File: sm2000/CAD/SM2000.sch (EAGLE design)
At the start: 360 parts, among them CN1 HDR100-3, CN10 ST-3509, CN11 HDR100-3, CN2 JS-MU3-002, CN3 DS-0518, CN5 ST-3509, CN8 ST-3509, J1 JMP-2PIN, J2 JMP-2PIN, J3 JMP-2PIN, J4 CONN-BOOM-XH-2A, P10 TPAD50, P11 TPAD50, P12 TPAD50, P13 TPAD50, P14 TPAD50, P16 TPAD50, P18 TPAD50, P19 TPAD50, P20 TPAD50, P21 TPAD50, P3 TPAD50, P4 TPAD50, P5 TPAD50, P6 TPAD50, P7 TPAD50, P8 TPAD50, P9 TPAD50, Q1 MMBT3904, Q12 BRF92, Q13 BFQ19, Q14 RD01MUS2, Q17 MMT2904, Q18 MMT2904, Q2 MMBT3904, Q3 MMBT3904, Q4 MMBT3904, Q5 MMBT3904, Q6 MMBT3904, Q7 BC548, Q8 BC549, SW1 SW-LC2259, SW2 TS-026, SW3 SW-LC2259EENP, SW4 TS-026, SW5 TS-02B, U1 STM32F405VGT6, U10 DNL, U12 PGA-103+, U13 ADE-1, U14 SI570CAC000141DG, U15 SI5351A, U3 STMPS2141, U4 EMIF02-USB03F2, U5 TPS54329E, U6 LD3985M33R, U7 SA612A, U8 LM386M-1, U9 LMV341, X1 BU-SMA-H, X2 BU-SMA-H

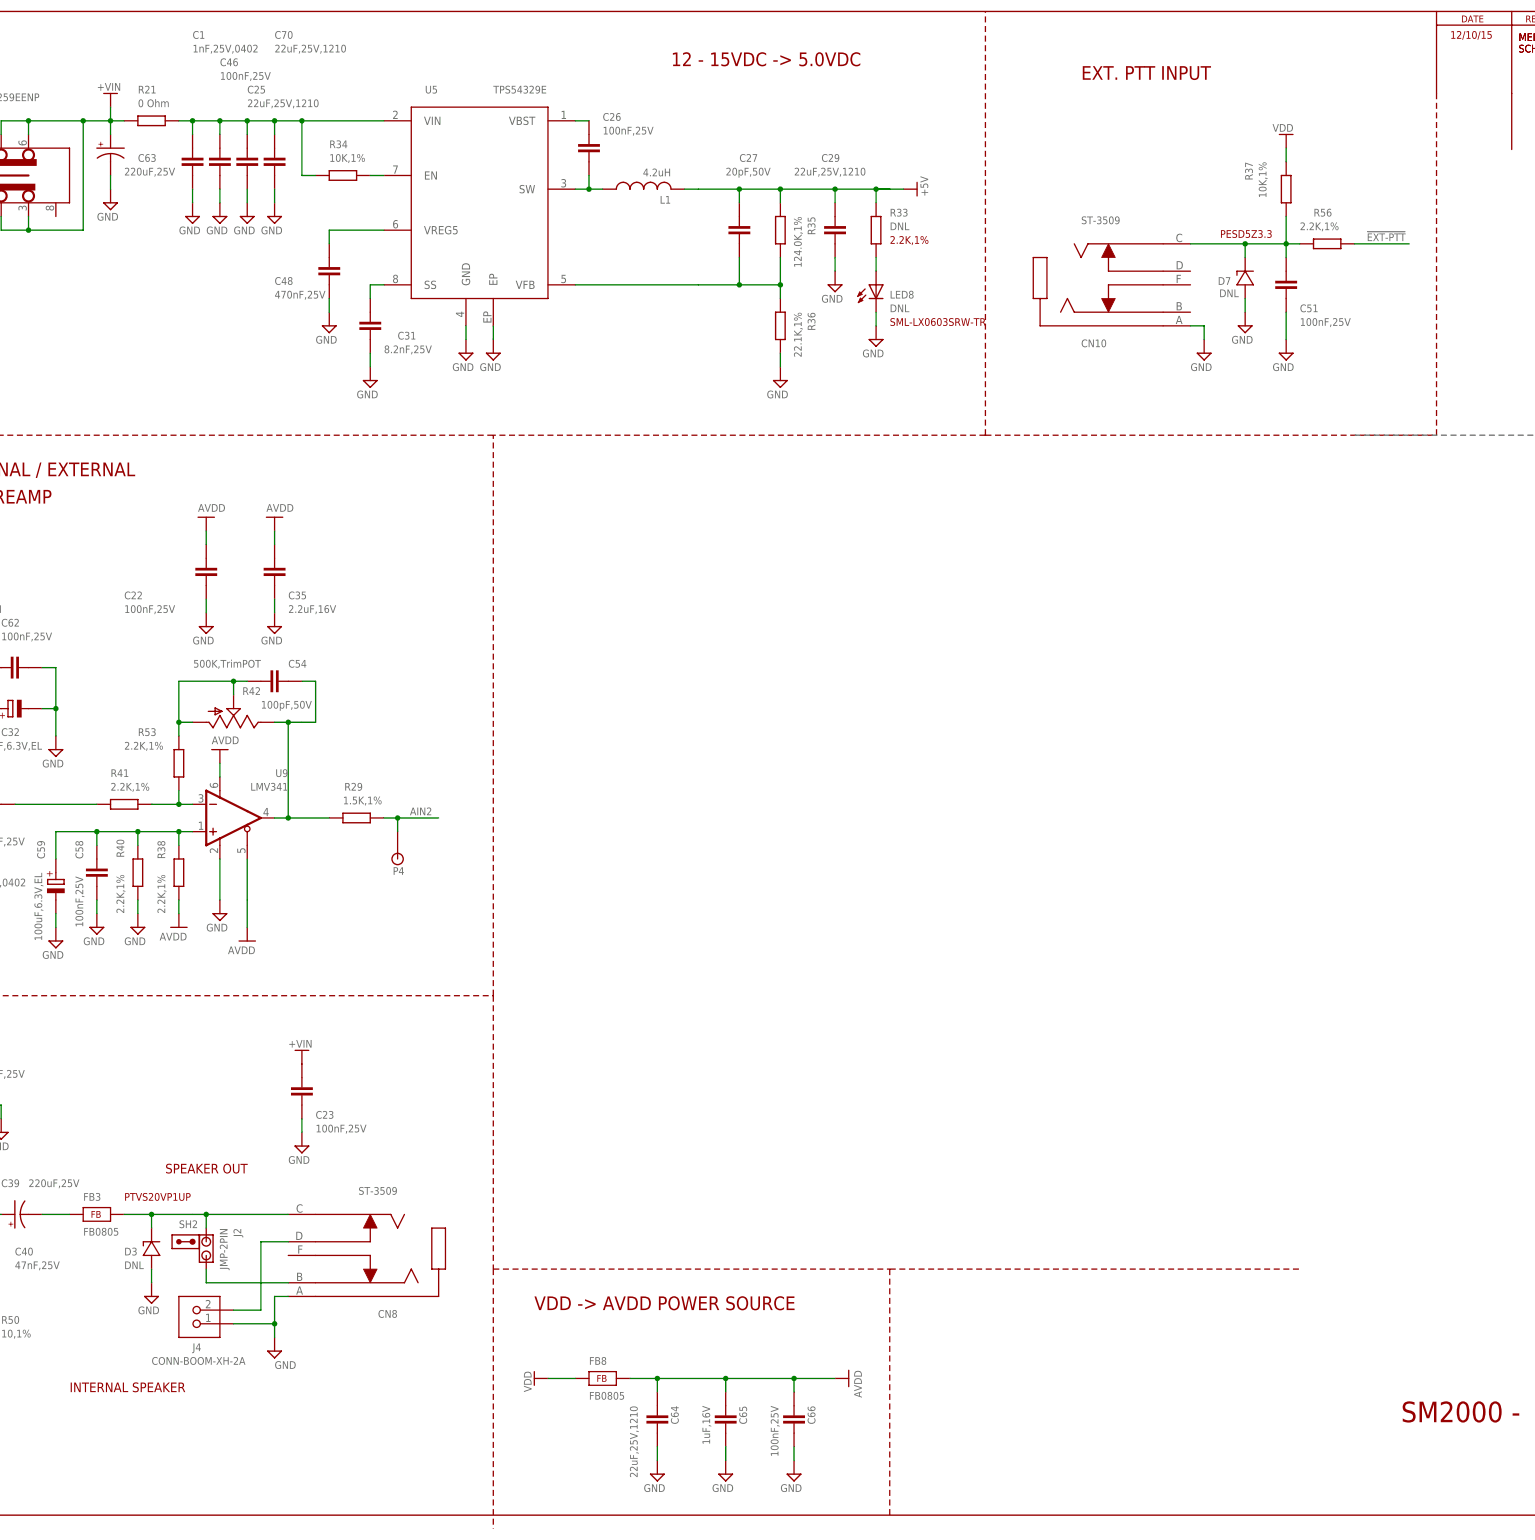
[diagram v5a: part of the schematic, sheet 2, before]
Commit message: Intermediate Schematic Cleanup Added +9, +5 & +3.3V regulators RGB
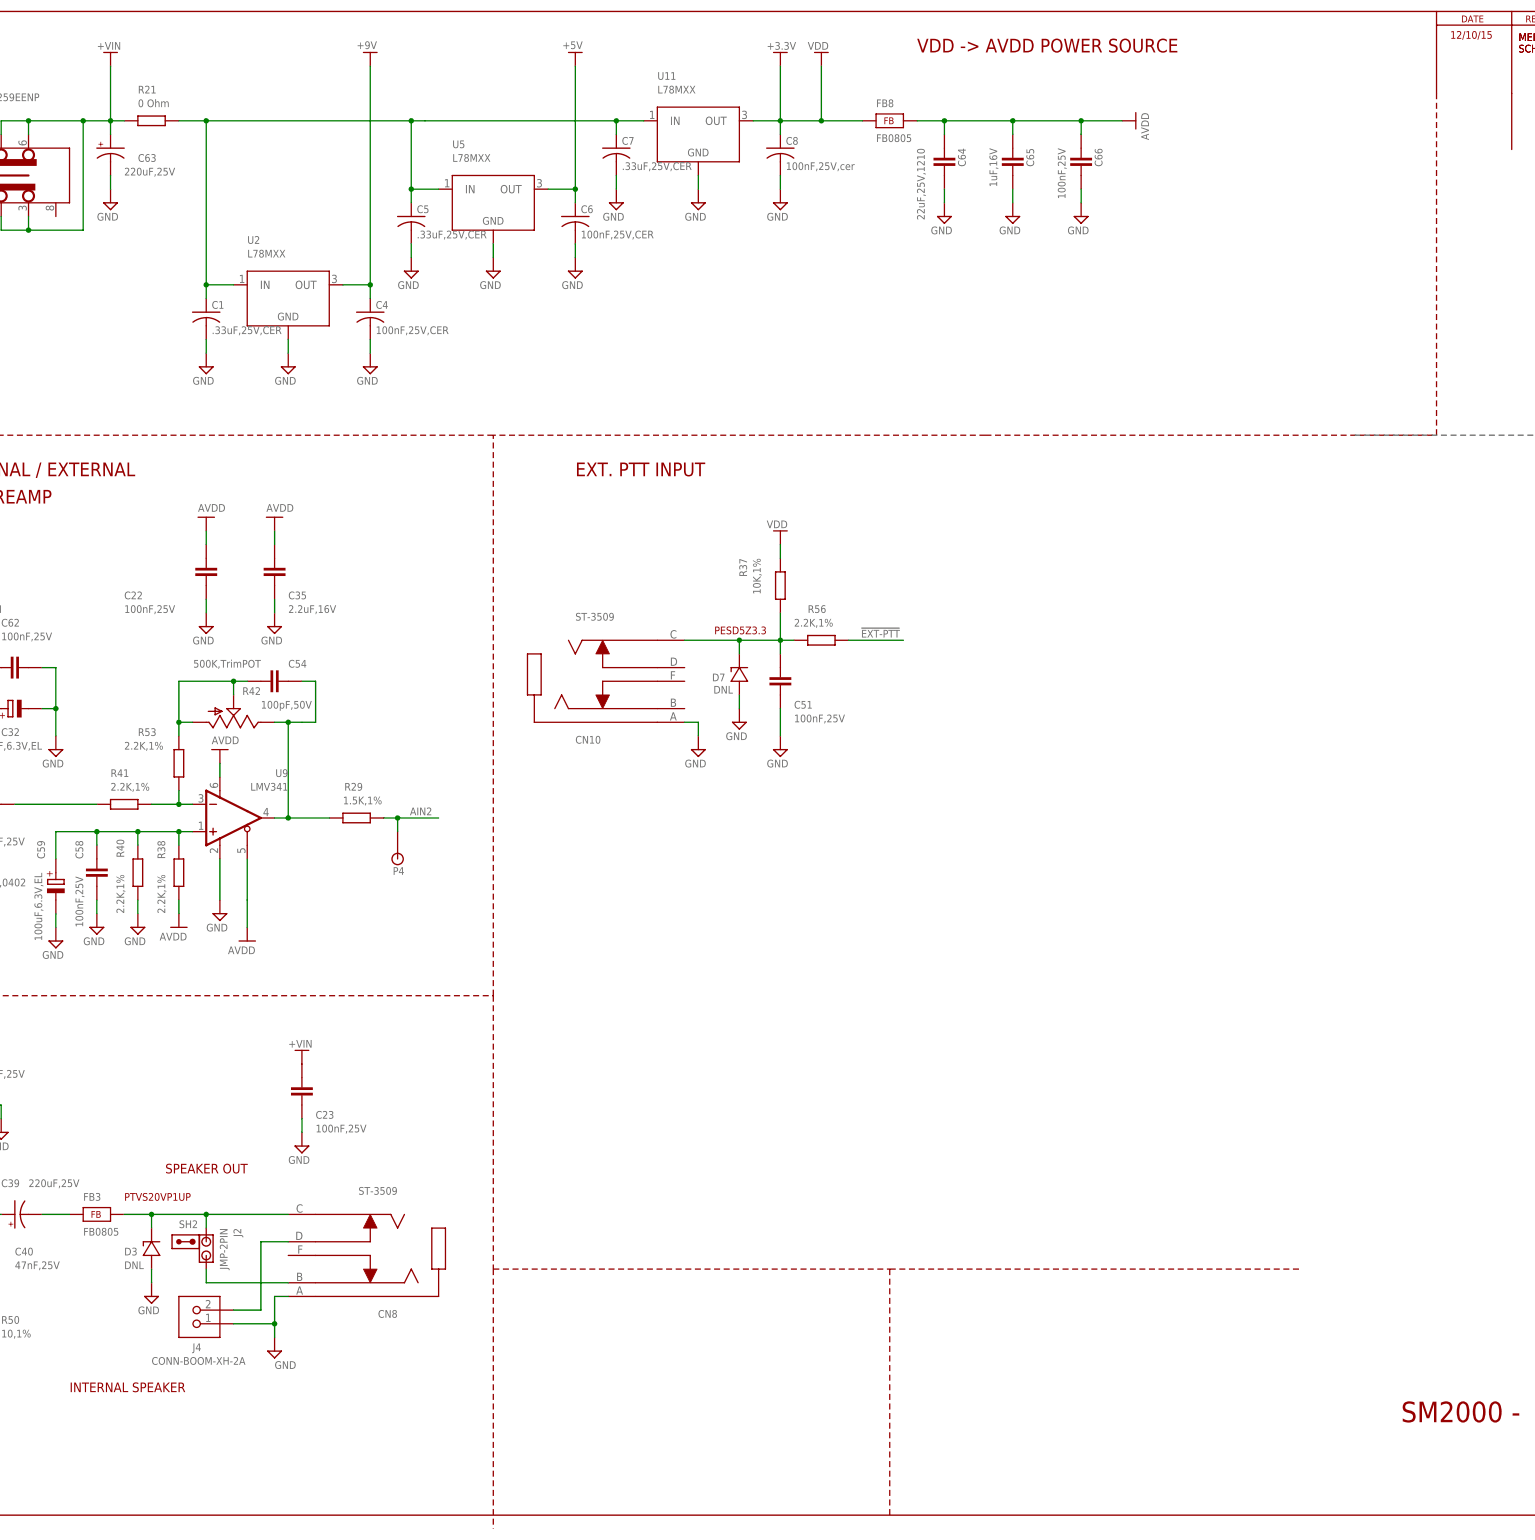
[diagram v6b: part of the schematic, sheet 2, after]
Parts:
- removed C25, C70: 22uF,25V,1210, ipc-7351-capacitor:CAPACITOR_1210
- removed C26, C46: 100nF,25V, AA-ipc-7351-capacitor:CAPACITOR_0402
- removed C27: 20pF,50V, AA-ipc-7351-capacitor:CAPACITOR_0402
- removed C29: 22uF,25V,1210, AA-ipc-7351-capacitor:CAPACITOR_1210
- removed C31: 8.2nF,25V, ipc-7351-capacitor:CAPACITOR_0603
- removed C48: 470nF,25V, ipc-7351-capacitor:CAPACITOR_0603
- removed L1: 4.2uH, _RoweTel:SRR5028
- removed LED8: DNL, _RoweTel:SML-LX0603SRW
- removed R33: DNL, AA-ipc-7351-resistor:RESISTOR_0402
- removed R34: 10K,1%, AA-ipc-7351-resistor:RESISTOR_0402
- removed R35: 124.0K,1%, AA-ipc-7351-resistor:RESISTOR_0402
- removed R36: 22.1K,1%, AA-ipc-7351-resistor:RESISTOR_0402
- added C4, C6: 100nF,25V,CER, _RoweTel:CAP-0805
- added C5, C7: .33uF,25V,CER, _RoweTel:CAP-0805
- added C8: 100nF,25V,cer, _RoweTel:CAP-0805
- added U11, U2: L78MXX, _RoweTel:L78MXX
- C1: value 1nF,25V,0402 -> .33uF,25V,CER; device AA-ipc-7351-capacitor:CAPACITOR_0402 -> _RoweTel:CAP-0805
- U5: value TPS54329E -> L78MXX; device _RoweTel:TPS54329E -> _RoweTel:L78MXX
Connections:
- removed net N$116: L13.1
- removed net N$138: C139.2
- removed net N$155: C147.1, R48.2
- removed net N$21: C26.1, U5.VBST
- removed net N$30: C27.2, R35.2, R36.1, U5.VFB
- removed net N$36: C1.2, C25.1, C46.1, C70.1, R21.2, R34.1, U5.VIN
- removed net N$38: C31.1, U5.SS
- removed net N$40: C48.1, U5.VREG5
- removed net N$42: R34.2, U5.EN
- removed net N$47: LED8.A, R33.2
- removed net N$50: U7.IN_B
- removed net SW: C26.2, L1.1, U5.SW
- new net +9V: C4.1, L13.1, U2.OUT
- new net ANT_SMA: C100.1, C147.1, L14.2, R48.2
- new net N$54: C1.1, C5.1, C7.1, R21.2, U11.IN, U2.IN, U5.IN
- net +5V: now also C6.1, U5.OUT; no longer C27.1, C29.1, L1.2, R33.1, R35.1
- net GND: now also C1.2, C4.2, C5.2, C6.2, C7.2, C8.2, U11.GND, U2.GND; no longer C1.1, C25.2, C29.2, C31.2, C46.2, C48.2, C70.2, LED8.C, R36.2, U5.EP
- net N$11: now also C139.2, U12.1N; no longer C100.1, L14.2
- net N$51: now also U7.IN_B
- net VDD: now also C8.1, U11.OUT
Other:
- note removed: "+9V"
- note removed: "12 - 15VDC -> 5.0VDC"
- note removed: "2.2K,1%"
- note removed: "Antenna SMA"
- moved on the sheet: C1, C135, C136, C51, C64, C65, C66, C97, CN10, D7, FB21, FB6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

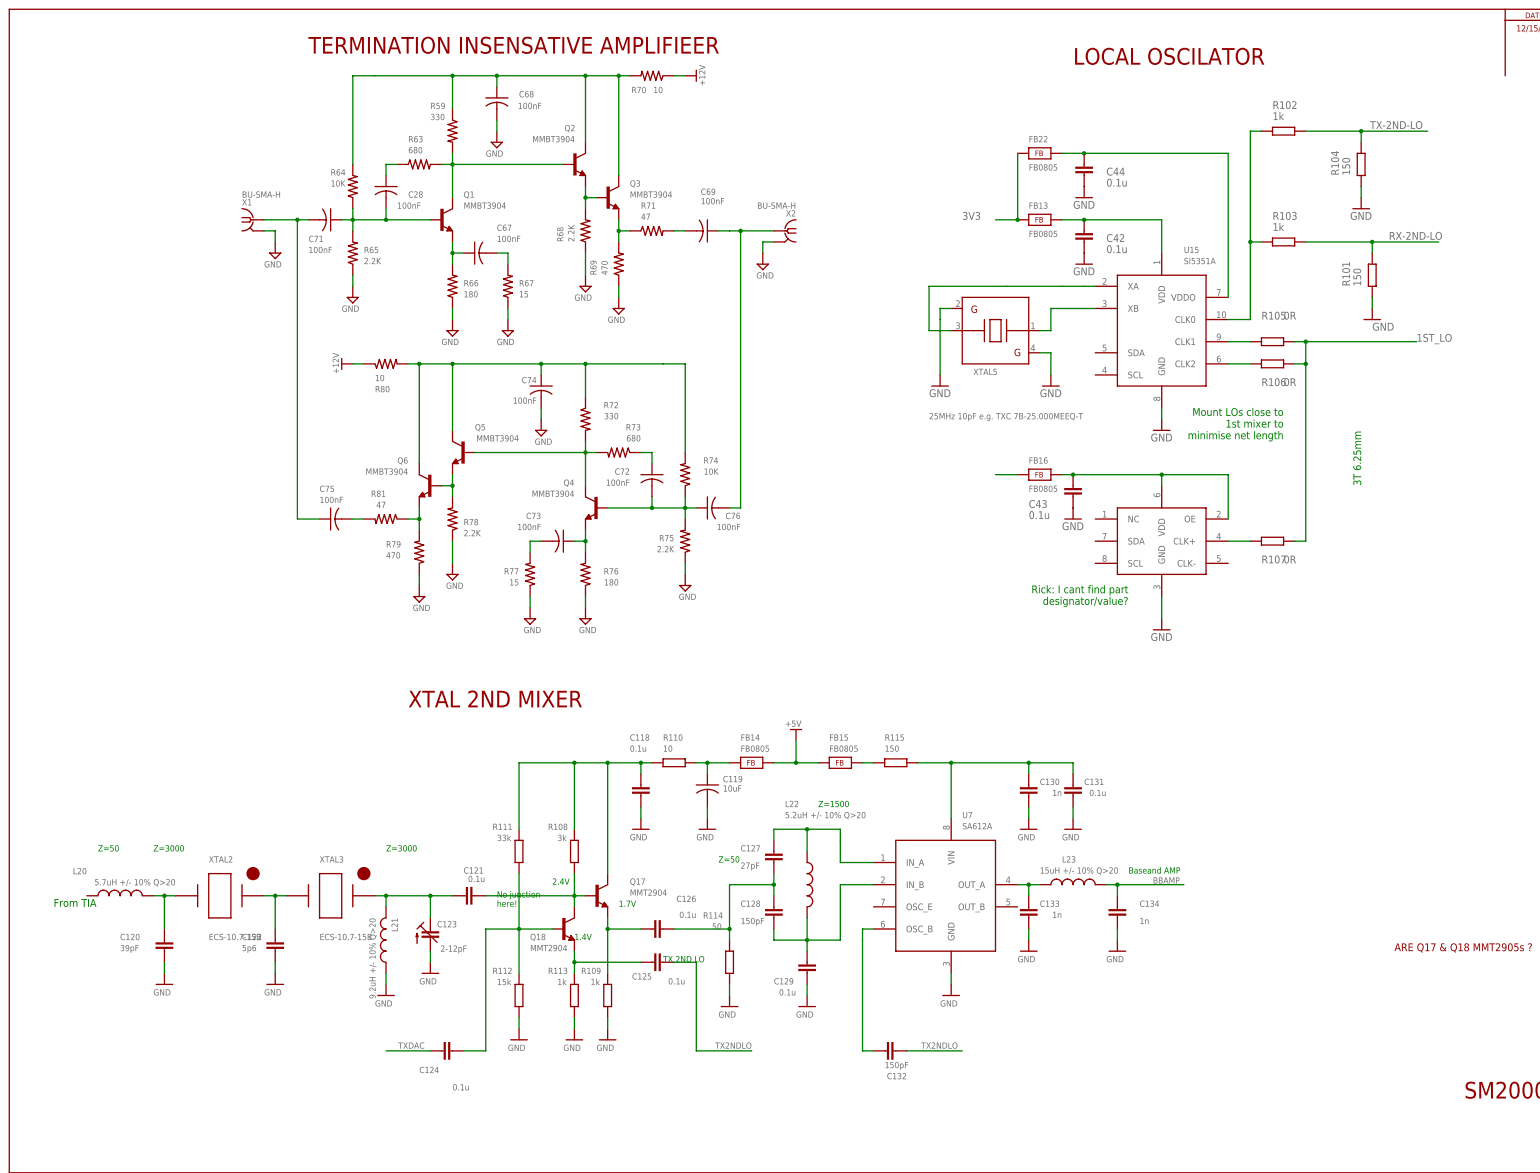
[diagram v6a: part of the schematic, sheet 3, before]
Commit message: Added Circuitry for +12_TX and +12V_RX. Need to add +12V_TX_ENB and +12V_RX_ENB to CPU. Used P-Channel mosfet for voltage SW and MMBT3904 to control sw(price). See Pg 3.
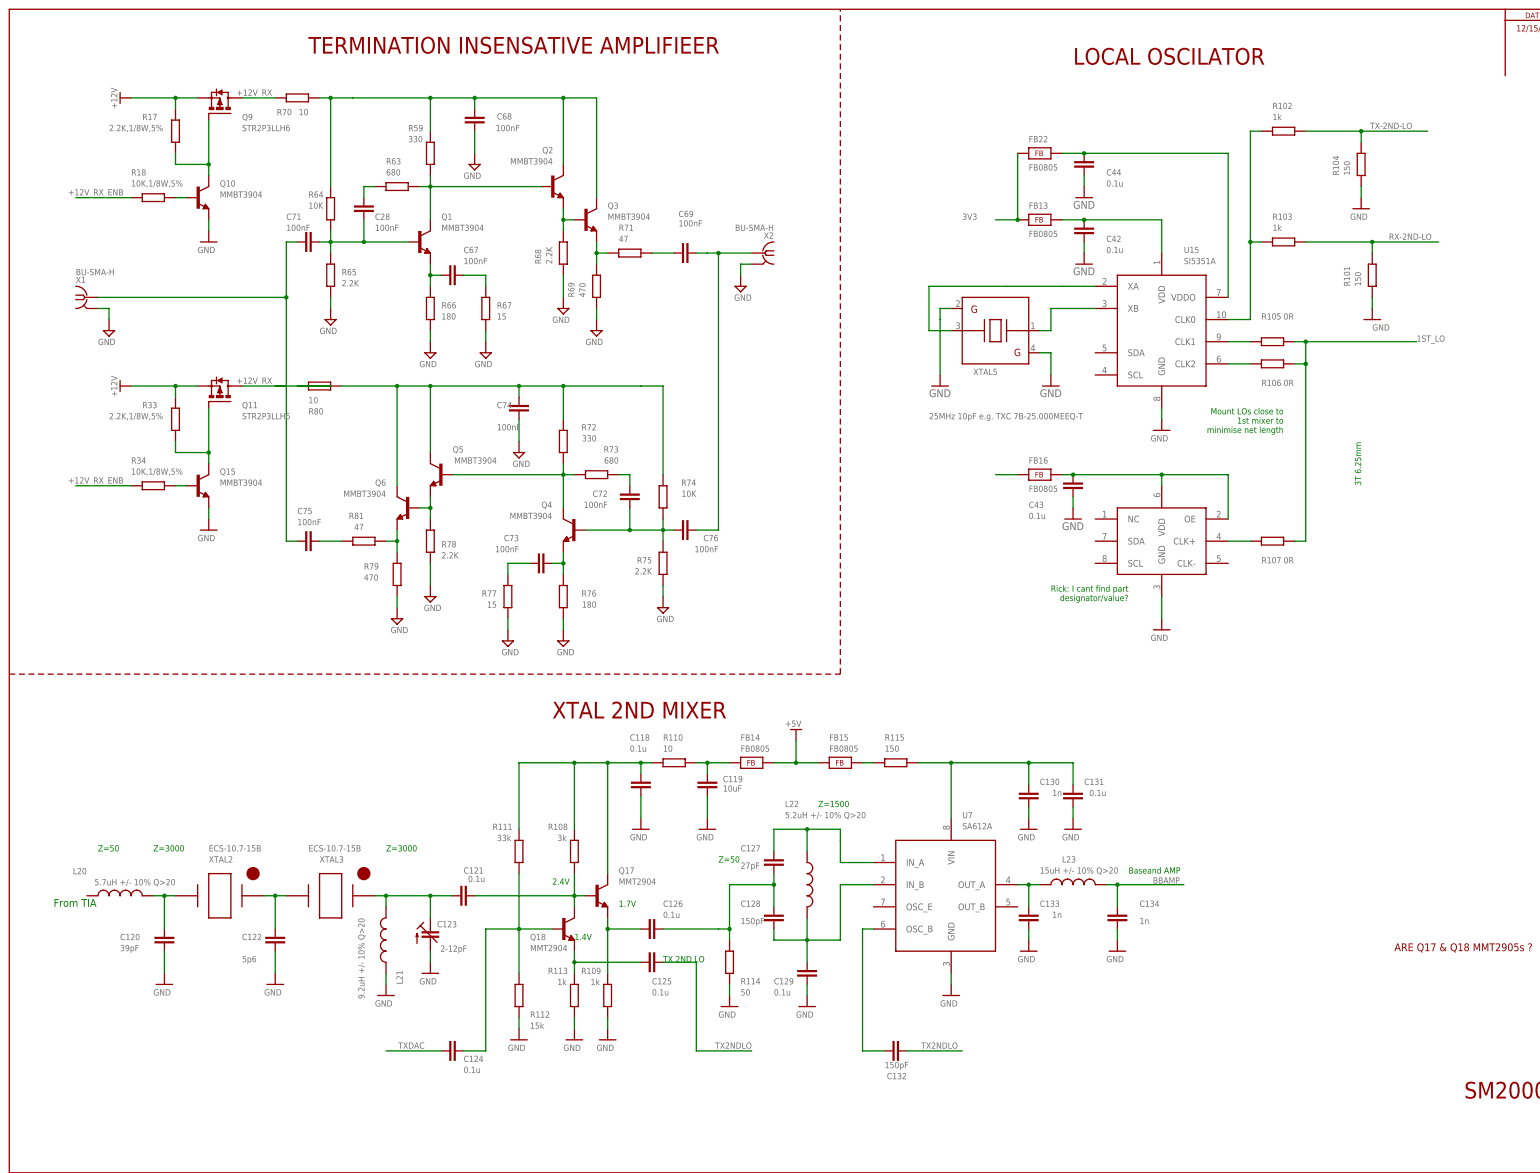
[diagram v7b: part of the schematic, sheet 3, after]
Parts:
- added Q10, Q15: MMBT3904, _RoweTel:MMBT3904
- added Q11, Q9: STR2P3LLH6, _RoweTel:STR2P3LLH6
- added R17, R33: 2.2K,1/8W,5%, _RoweTel:RES-0805
- added R18, R34: 10K,1/8W,5%, _RoweTel:RES-0805
- C1, C5, C7: value .33uF,25V,CER -> .33uF,25V
- C10, C12, C14, C15, C24, C35, C36, C47, C65: device AA-ipc-7351-capacitor:CAPACITOR_0603 -> _RoweTel:CAP-0805
- C100, C118, C120, C121, C122, C124, C125, C126, C127, C128, C129, C130, C131, C132, C133, C134, C42, C43, C44, C77, C78, C88, C89, C90, C91, C92, C93, C95, C96, C97, C98, C99: device rcl:C-EU025-024X044 -> _RoweTel:CAP-0805
- C11, C13, C16, C17, C18, C19, C2, C20, C21, C22, C23, C3, C30, C33, C34, C38, C40, C41, C45, C49, C51, C52, C53, C54, C58, C62, C66: device AA-ipc-7351-capacitor:CAPACITOR_0402 -> _RoweTel:CAP-0805
- C110, C111, C112, C113, C114, C115, C116, C117, C135, C137, C138, C139, C140, C141, C142, C143, C144, C145, C146, C147, C148, C149, C87: device AA-ipc-7351-capacitor:CAPACITOR_0805 -> _RoweTel:CAP-0805
- C119, C79, C80, C81, C82: device _RoweTel:CAP-1210 -> _RoweTel:CAP-0805
- C4, C6: value 100nF,25V,CER -> 100nF,25V
- C55, C56: value 1nF,25V,0402 -> 1nF,25V; device AA-ipc-7351-capacitor:CAPACITOR_0402 -> _RoweTel:CAP-0805
- C57: value 3.9nF,16V,0402 -> 3.9nF,16V; device AA-ipc-7351-capacitor:CAPACITOR_0402 -> _RoweTel:CAP-0805
- C64: value 22uF,25V,1210 -> 22uF,25V; device AA-ipc-7351-capacitor:CAPACITOR_1210 -> _RoweTel:CAP-0805
- C8: value 100nF,25V,cer -> 100nF,25V
- R1, R12, R13, R14, R15, R16, R2, R24, R25, R27, R28, R3, R4, R5, R6, R7, R8, R9: device AA-ipc-7351-resistor:RESISTOR_0402 -> _RoweTel:RES-0805
- R10, R19, R20, R23, R26, R30, R31, R54, R61, R62: device AA-ipc-7351-resistor:RESISTOR_0603 -> _RoweTel:RES-0805
- R101, R102, R103, R104, R105, R106, R107, R108, R109, R110, R111, R112, R113, R114, R115, R55, R60, R82, R83, R84, R85, R86, R87, R88, R89, R90, R91, R92, R93, R94, R95, R96, R97, R98, R99: device AA-ipc-7351-resistor:RESISTOR_0805 -> _RoweTel:RES-0805
- R45, R47, R48, R49, R59, R63, R64, R65, R66, R67, R68, R69, R70, R71, R72, R73, R74, R75, R76, R77, R78, R79, R80, R81: device _RoweTel:RES0805 -> _RoweTel:RES-0805
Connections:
- new net +12V_RX: Q11.D, Q9.D, R70.2
- new net +12V_RX_ENB: R18.1, R34.1
- new net N$30: C144.1
- new net N$36: C143.2
- new net N$38: C137.2
- new net N$40: R80.1
- new net N$42: Q10.C, Q9.G, R17.1
- new net N$50: Q11.G, Q15.C, R33.1
- new net N$53: Q10.B, R18.2
- new net N$55: Q15.B, R34.2
- net +12V: now also Q11.S, Q9.S, R17.2, R33.2; no longer R70.1, R80.1
- net GND: now also Q10.E, Q15.E
- net N$67: now also R70.1; no longer R70.2
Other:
- note removed: "No junction here!"
- moved on the sheet: C136, D10, D11, D12, D13, FB17, FB18, FB19, FB20, FB21, L16, L17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
